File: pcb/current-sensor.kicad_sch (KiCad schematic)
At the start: 37 parts, among them U1 SS39ET, U2 TLV9064, U3 SS39ET

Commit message: Set stackup; added pics to root; minor graphics editing; fixed models
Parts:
- C1, C10, C4, C5: LCSC C713509 -> C106217; MN CCTC -> Yageo; MPN TCC0603Y5V224M500CT -> CC0603KRX7R8BB223
- C7: MN YAGEO -> Yageo
- R3, R4, R9: LCSC C103676 -> C2933228; MN RALEC -> FOJAN; MPN RTT034991FTP -> FRC0603F4991TS
- RV1: footprint Potentiometer_SMD:Potentiometer_Bourns_TC33X_Vertical -> CRGM Passive:Bourns_TC33X_Vertical; symbol Device:R_Potentiometer_US -> CRGM Passive:R_Potentiometer_US
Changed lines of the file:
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@@
 	)
 	(symbol
-		(lib_id "Device:R_Potentiometer_US")
+		(lib_id "CRGM Passive:R_Potentiometer_US")
 		(at 214.63 35.56 90)
 		(unit 1)
@@
 			)
 		)
-		(property "Footprint" "Potentiometer_SMD:Potentiometer_Bourns_TC33X_Vertical"
+		(property "Footprint" "CRGM Passive:Bourns_TC33X_Vertical"
 			(at 214.63 35.56 0)
 			(effects
@@
 			)
 		)
-		(property "Description" "±25% ±250ppm/℃ 100mW 1MΩ SMD-3P,3.8x3.6mm Potentiometers"
-			(at 214.63 35.56 0)
+		(property "Description" "Potentiometer, US symbol"
+			(at 226.314 35.56 0)
 			(effects
 				(font
@@
 			)
 		)
-		(property "MN" "CCTC"
+		(property "MN" "Yageo"
 			(at 162.56 71.12 0)
 			(effects
@@
 			)
 		)
-		(property "MPN" "TCC0603Y5V224M500CT"
+		(property "MPN" "CC0603KRX7R8BB223"
 			(at 162.56 71.12 0)
 			(effects
@@
 			)
 		)
-		(property "LCSC" "C713509"
+		(property "LCSC" "C106217"
 			(at 162.56 71.12 0)
 			(effects
@@
 			)
 		)
-		(property "MPN" "RTT034991FTP"
+		(property "MPN" "FRC0603F4991TS"
 			(at 86.36 53.34 0)
 			(effects
@@
 			)
 		)
-		(property "MN" "RALEC"
+		(property "MN" "FOJAN"
 			(at 86.36 53.34 90)
 			(effects
@@
 			)
 		)
-		(property "LCSC" "C103676"
+		(property "LCSC" "C2933228"
 			(at 86.36 53.34 0)
 			(effects
@@
 			)
 		)
-		(property "MN" "CCTC"
+		(property "MN" "Yageo"
 			(at 194.31 77.47 0)
 			(effects
@@
 			)
 		)
-		(property "MPN" "TCC0603Y5V224M500CT"
+		(property "MPN" "CC0603KRX7R8BB223"
 			(at 194.31 77.47 0)
 			(effects
@@
 			)
 		)
-		(property "LCSC" "C713509"
+		(property "LCSC" "C106217"
 			(at 194.31 77.47 0)
 			(effects
@@
 			)
 		)
-		(property "MPN" "RTT034991FTP"
+		(property "MPN" "FRC0603F4991TS"
 			(at 85.09 81.28 0)
 			(effects
@@
 			)
 		)
-		(property "MN" "RALEC"
+		(property "MN" "FOJAN"
 			(at 85.09 81.28 90)
 			(effects
@@
 			)
 		)
-		(property "LCSC" "C103676"
+		(property "LCSC" "C2933228"
 			(at 85.09 81.28 0)
 			(effects
@@
 			)
 		)
-		(property "MN" " YAGEO"
+		(property "MN" "Yageo"
 			(at 111.76 81.28 0)
 			(effects
@@
 			)
 		)
-		(property "MN" "CCTC"
+		(property "MN" "Yageo"
 			(at 146.05 154.94 0)
 			(effects
@@
 			)
 		)
-		(property "MPN" "TCC0603Y5V224M500CT"
+		(property "MPN" "CC0603KRX7R8BB223"
 			(at 146.05 154.94 0)
 			(effects
@@
 			)
 		)
-		(property "LCSC" "C713509"
+		(property "LCSC" "C106217"
 			(at 146.05 154.94 0)
 			(effects
@@
 			)
 		)
-		(property "MPN" "RTT034991FTP"
+		(property "MPN" "FRC0603F4991TS"
 			(at 187.96 58.42 0)
 			(effects
@@
 			)
 		)
-		(property "MN" "RALEC"
+		(property "MN" "FOJAN"
 			(at 187.96 58.42 90)
 			(effects
@@
 			)
 		)
-		(property "LCSC" "C103676"
+		(property "LCSC" "C2933228"
 			(at 187.96 58.42 0)
 			(effects
@@
 			)
 		)
-		(property "MN" "CCTC"
+		(property "MN" "Yageo"
 			(at 208.28 41.91 0)
 			(effects
@@
 			)
 		)
-		(property "MPN" "TCC0603Y5V224M500CT"
+		(property "MPN" "CC0603KRX7R8BB223"
 			(at 208.28 41.91 0)
 			(effects
@@
 			)
 		)
-		(property "LCSC" "C713509"
+		(property "LCSC" "C106217"
 			(at 208.28 41.91 0)
 			(effects

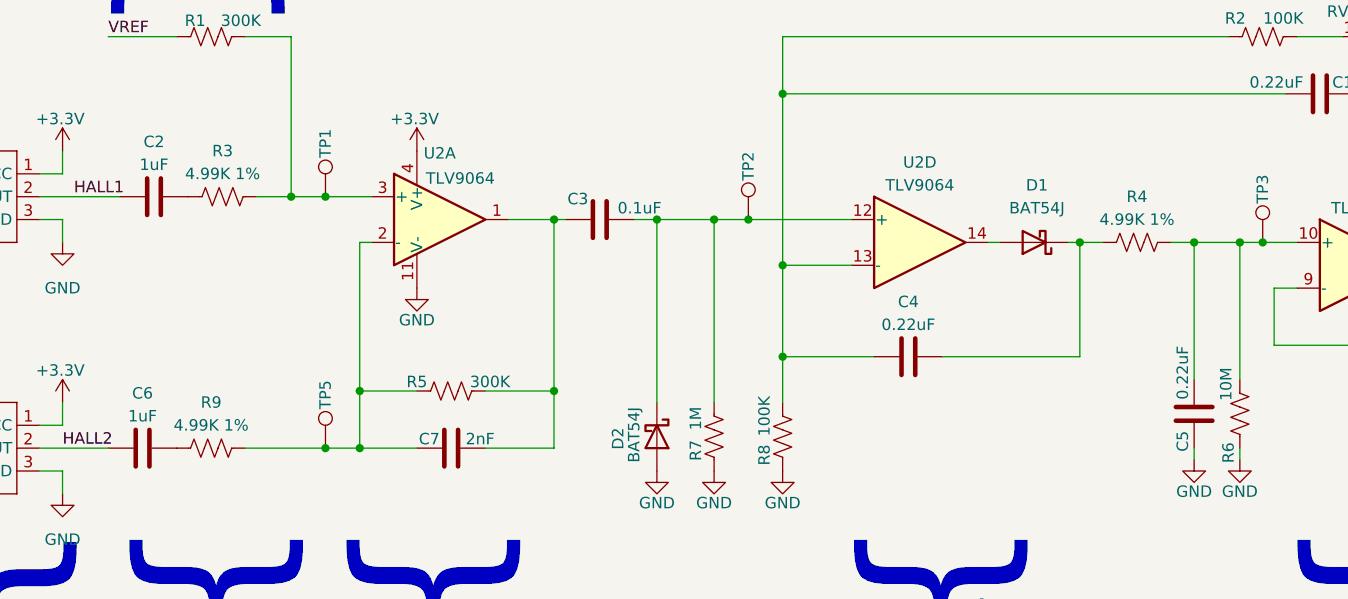
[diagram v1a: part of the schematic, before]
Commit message: Fixed production errors
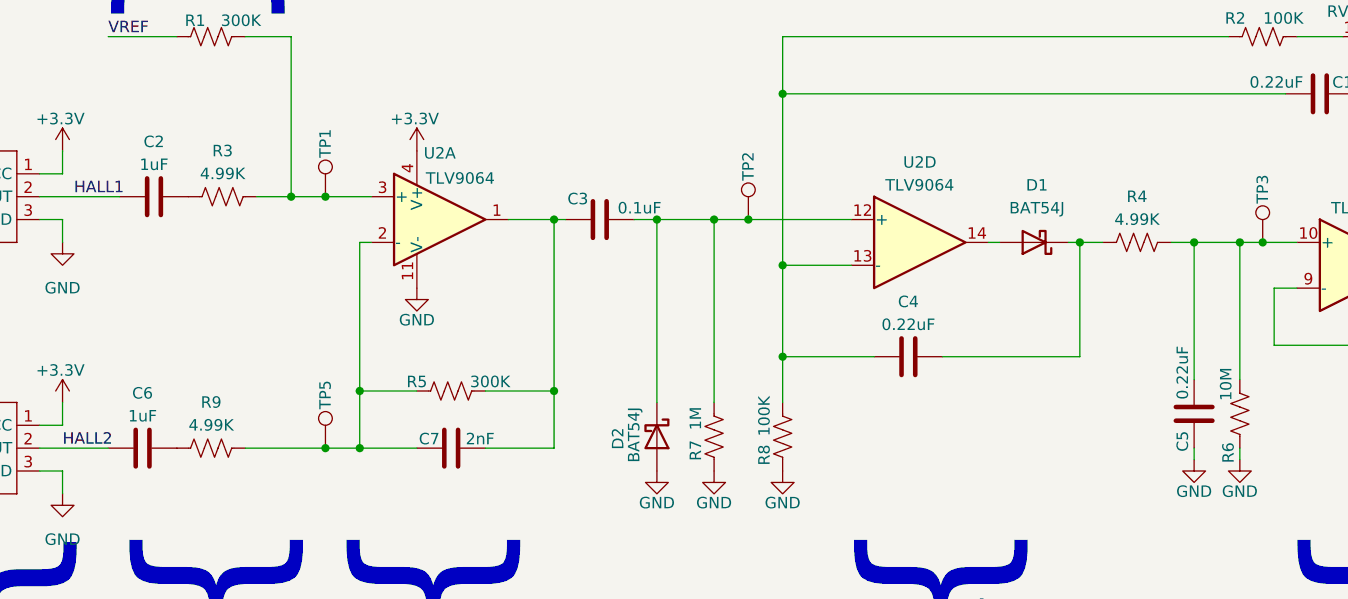
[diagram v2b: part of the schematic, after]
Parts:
- C2, C6: Digikey 1276-1019-2-ND -> 1276-1019-2-ND
- J1: Digikey 455-SM03B-SRSS-TBTR-ND -> 455-SM03B-SRSS-TBTR-ND
- R3, R4, R9: value 4.99K 1% -> 4.99K; Tolerance (none) -> 1%
- RV1: MN BOURNS -> BOURNS
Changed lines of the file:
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@@
 			)
 		)
-		(property "Digikey" "1276-1019-2-ND "
+		(property "Digikey" "1276-1019-2-ND"
 			(at 77.47 81.28 90)
 			(effects
@@
 			)
 		)
-		(property "MN" " BOURNS"
+		(property "MN" "BOURNS"
 			(at 214.63 35.56 0)
 			(effects
@@
 			)
 		)
-		(property "Value" "4.99K 1%"
+		(property "Value" "4.99K"
 			(at 86.36 50.8 90)
 			(effects
@@
 			)
 		)
+		(property "Tolerance" "1%"
+			(at 86.36 53.34 90)
+			(effects
+				(font
+					(size 1.27 1.27)
+				)
+				(hide yes)
+			)
+		)
 		(pin "2"
 		)
@@
 			)
 		)
-		(property "Digikey" "455-SM03B-SRSS-TBTR-ND "
+		(property "Digikey" "455-SM03B-SRSS-TBTR-ND"
 			(at 247.65 55.88 0)
 			(effects
@@
 			)
 		)
-		(property "Value" "4.99K 1%"
+		(property "Value" "4.99K"
 			(at 85.09 78.74 90)
 			(effects
@@
 			)
 		)
+		(property "Tolerance" "1%"
+			(at 85.09 81.28 90)
+			(effects
+				(font
+					(size 1.27 1.27)
+				)
+				(hide yes)
+			)
+		)
 		(pin "2"
 		)
@@
 			)
 		)
-		(property "Digikey" "1276-1019-2-ND "
+		(property "Digikey" "1276-1019-2-ND"
 			(at 78.74 53.34 90)
 			(effects
@@
 			)
 		)
-		(property "Value" "4.99K 1%"
+		(property "Value" "4.99K"
 			(at 187.96 55.88 90)
 			(effects
@@
 			(at 187.96 58.42 90)
 			(effects
+				(font
+					(size 1.27 1.27)
+				)
+				(hide yes)
+			)
+		)
+		(property "Tolerance" "1%"
+			(at 187.96 58.42 90)
+			(effects

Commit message: Changed resistor and cap footprints to CRGM
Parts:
- C1, C10, C11, C2, C3, C4, C5, C6, C7, C8, C9: footprint Capacitor_SMD:C_0603_1608Metric -> CRGM Passive:C_0603_1608Metric
- R1, R10, R11, R2, R3, R4, R5, R6, R7, R8, R9: footprint Resistor_SMD:R_0603_1608Metric -> CRGM Passive:R_0603_1608Metric
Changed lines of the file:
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@@
 			)
 		)
-		(property "Footprint" "Capacitor_SMD:C_0603_1608Metric"
+		(property "Footprint" "CRGM Passive:C_0603_1608Metric"
 			(at 132.08 54.9148 0)
 			(effects
@@
 			)
 		)
-		(property "Footprint" "Capacitor_SMD:C_0603_1608Metric"
+		(property "Footprint" "CRGM Passive:C_0603_1608Metric"
 			(at 81.28 80.3148 0)
 			(effects
@@
 			)
 		)
-		(property "Footprint" "Resistor_SMD:R_0603_1608Metric"
+		(property "Footprint" "CRGM Passive:R_0603_1608Metric"
 			(at 39.116 164.084 90)
 			(effects
@@
 			)
 		)
-		(property "Footprint" "Capacitor_SMD:C_0603_1608Metric"
+		(property "Footprint" "CRGM Passive:C_0603_1608Metric"
 			(at 166.37 70.1548 0)
 			(effects
@@
 			)
 		)
-		(property "Footprint" "Capacitor_SMD:C_0603_1608Metric"
+		(property "Footprint" "CRGM Passive:C_0603_1608Metric"
 			(at 108.9152 158.75 0)
 			(effects
@@
 			)
 		)
-		(property "Footprint" "Resistor_SMD:R_0603_1608Metric"
+		(property "Footprint" "CRGM Passive:R_0603_1608Metric"
 			(at 86.106 54.356 90)
 			(effects
@@
 			)
 		)
-		(property "Footprint" "Capacitor_SMD:C_0603_1608Metric"
+		(property "Footprint" "CRGM Passive:C_0603_1608Metric"
 			(at 193.3448 73.66 0)
 			(effects
@@
 			)
 		)
-		(property "Footprint" "Resistor_SMD:R_0603_1608Metric"
+		(property "Footprint" "CRGM Passive:R_0603_1608Metric"
 			(at 39.116 146.304 90)
 			(effects
@@
 			)
 		)
-		(property "Footprint" "Resistor_SMD:R_0603_1608Metric"
+		(property "Footprint" "CRGM Passive:R_0603_1608Metric"
 			(at 84.836 82.296 90)
 			(effects
@@
 			)
 		)
-		(property "Footprint" "Resistor_SMD:R_0603_1608Metric"
+		(property "Footprint" "CRGM Passive:R_0603_1608Metric"
 			(at 200.406 77.724 90)
 			(effects
@@
 			)
 		)
-		(property "Footprint" "Capacitor_SMD:C_0603_1608Metric"
+		(property "Footprint" "CRGM Passive:C_0603_1608Metric"
 			(at 115.57 80.3148 0)
 			(effects
@@
 			)
 		)
-		(property "Footprint" "Capacitor_SMD:C_0603_1608Metric"
+		(property "Footprint" "CRGM Passive:C_0603_1608Metric"
 			(at 119.0752 158.75 0)
 			(effects
@@
 			)
 		)
-		(property "Footprint" "Capacitor_SMD:C_0603_1608Metric"
+		(property "Footprint" "CRGM Passive:C_0603_1608Metric"
 			(at 31.4452 167.64 0)
 			(effects
@@
 			)
 		)
-		(property "Footprint" "Resistor_SMD:R_0603_1608Metric"
+		(property "Footprint" "CRGM Passive:R_0603_1608Metric"
 			(at 111.506 75.946 90)
 			(effects
@@
 			)
 		)
-		(property "Footprint" "Resistor_SMD:R_0603_1608Metric"
+		(property "Footprint" "CRGM Passive:R_0603_1608Metric"
 			(at 149.606 80.264 90)
 			(effects
@@
 			)
 		)
-		(property "Footprint" "Resistor_SMD:R_0603_1608Metric"
+		(property "Footprint" "CRGM Passive:R_0603_1608Metric"
 			(at 84.836 36.576 90)
 			(effects
@@
 			)
 		)
-		(property "Footprint" "Capacitor_SMD:C_0603_1608Metric"
+		(property "Footprint" "CRGM Passive:C_0603_1608Metric"
 			(at 147.0152 158.75 0)
 			(effects
@@
 			)
 		)
-		(property "Footprint" "Resistor_SMD:R_0603_1608Metric"
+		(property "Footprint" "CRGM Passive:R_0603_1608Metric"
 			(at 141.986 80.264 90)
 			(effects
@@
 			)
 		)
-		(property "Footprint" "Capacitor_SMD:C_0603_1608Metric"
+		(property "Footprint" "CRGM Passive:C_0603_1608Metric"
 			(at 82.55 52.3748 0)
 			(effects
@@
 			)
 		)
-		(property "Footprint" "Resistor_SMD:R_0603_1608Metric"
+		(property "Footprint" "CRGM Passive:R_0603_1608Metric"
 			(at 187.706 59.436 90)
 			(effects
@@
 			)
 		)
-		(property "Footprint" "Capacitor_SMD:C_0603_1608Metric"
+		(property "Footprint" "CRGM Passive:C_0603_1608Metric"
 			(at 212.09 40.9448 0)
 			(effects
@@
 			)
 		)
-		(property "Footprint" "Resistor_SMD:R_0603_1608Metric"
+		(property "Footprint" "CRGM Passive:R_0603_1608Metric"
 			(at 201.676 36.576 90)
 			(effects
